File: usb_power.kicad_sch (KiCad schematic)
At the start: 13 parts, among them J1 USB_C_Receptacle_USB2.0_14P, U12 CH340N, U13 TP4056-42-ESOP8

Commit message: HW: Update schematic info frames
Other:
- company: (none) -> A.K.
- title: (none) -> USB and power management
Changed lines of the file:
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@@
 	(generator_version "9.0")
 	(paper "A4")
+	(title_block
+		(title "USB and power management")
+		(date "2025-10-14")
+		(rev "A")
+		(company "A.K.")
+	)
 	(text "TODO:\n\nBattery connector\nDCDC"
 		(exclude_from_sim no)

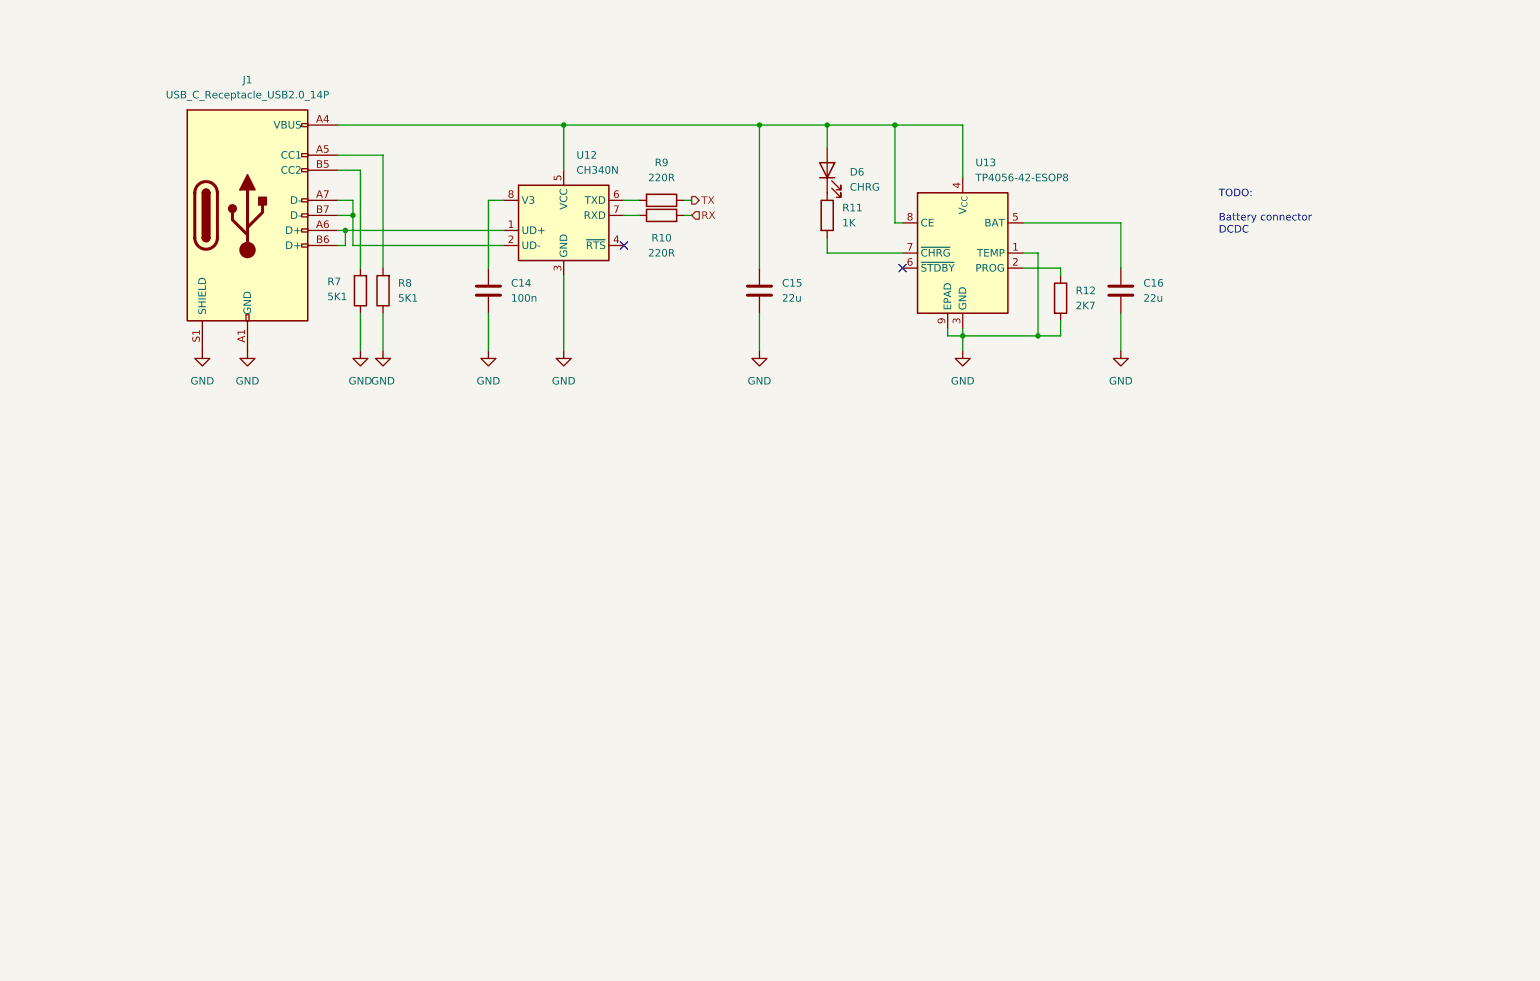
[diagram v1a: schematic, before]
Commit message: HW: Add DC-DC step-up converter
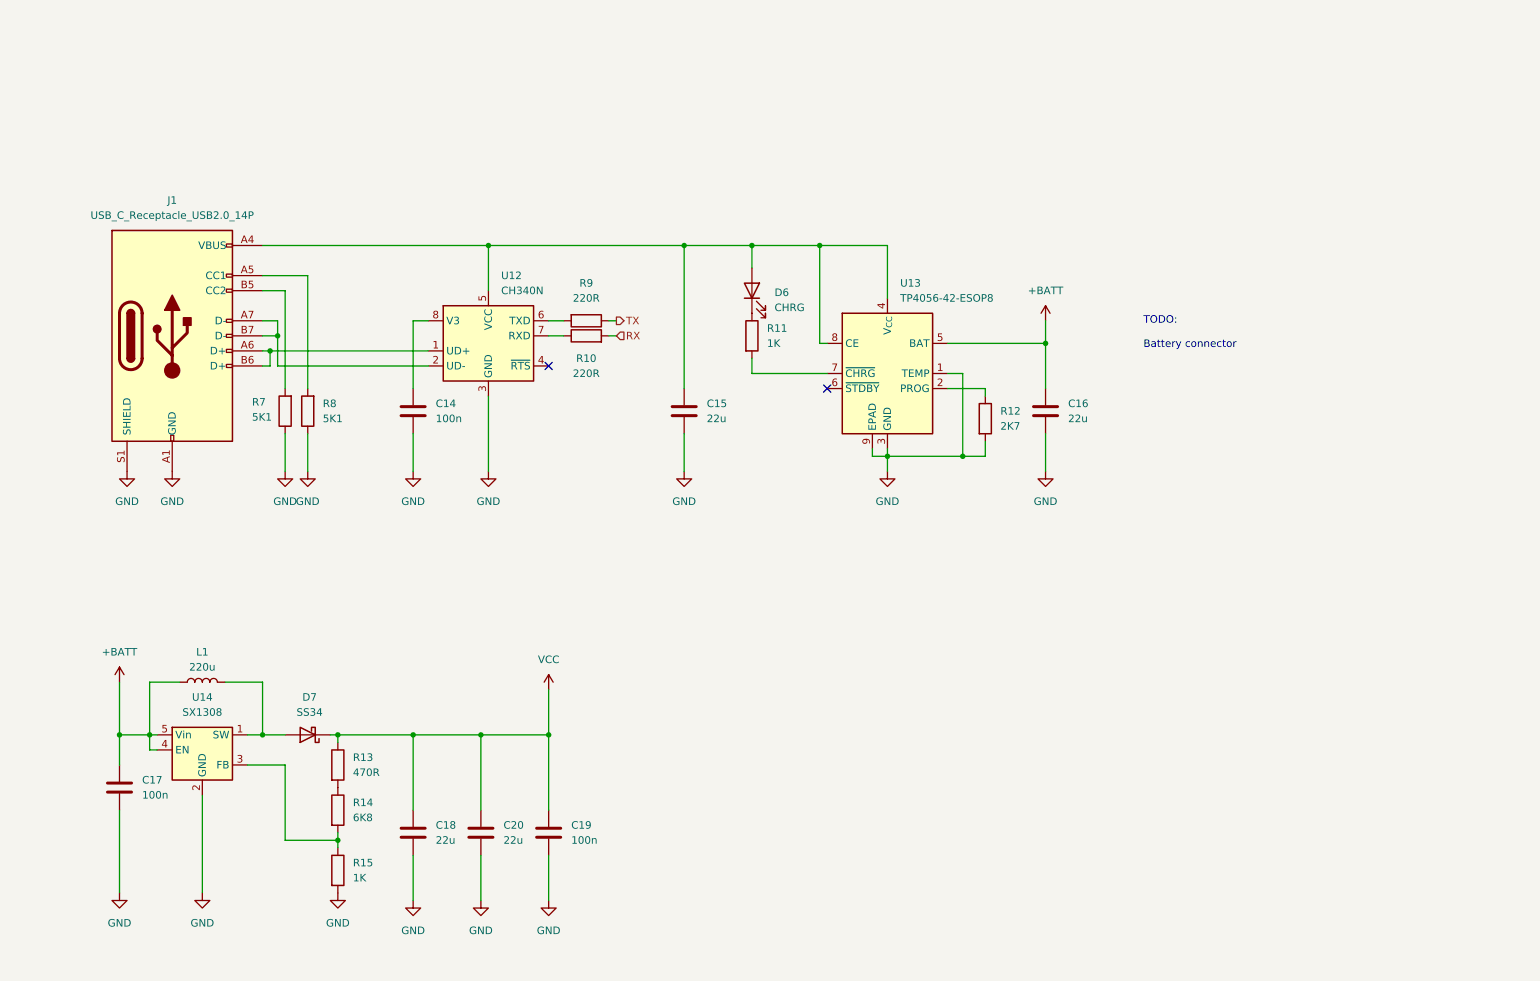
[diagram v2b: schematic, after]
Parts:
- added C17, C19: 100n, Capacitor_SMD:C_0805_2012Metric, symbol Device:C
- added C18, C20: 22u, Capacitor_SMD:C_0805_2012Metric, symbol Device:C
- added D7: SS34, Diode_SMD:D_2010_5025Metric, symbol Device:D_Schottky
- added L1: 220u, Inductor_SMD:L_Sunlord_SWPA6040S, symbol Device:L
- added R13: 470R, Resistor_SMD:R_0805_2012Metric, symbol Device:R
- added R14: 6K8, Resistor_SMD:R_0805_2012Metric, symbol Device:R
- added R15: 1K, Resistor_SMD:R_0805_2012Metric, symbol Device:R
- added U14: SX1308, Package_TO_SOT_SMD:TSOT-23-5, symbol Regulator_Switching:ADP2108AUJ-3.3
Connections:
- net GND: now also C17.1, C18.2, C19.2, C20.2, R15.2, U14.2 (GND)
- net +BATT: now reaches C16.1, U13.5 (BAT)
- net +BATT: now also C17.2, L1.1, U14.4 (EN), U14.5 (Vin)
- new net: R14.2, R15.1, U14.3 (FB)
- new net: D7.2 (A), L1.2, U14.1 (SW)
- new net: R13.2, R14.1
- new net VCC: C18.1, C19.1, C20.1, D7.1 (K), R13.1
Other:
- note added: "TODO: Battery connector"
- note removed: "TODO: Battery connector DCDC"
- moved on the sheet: C14, C15, C16, D6, J1, R10, R11, R12, R7, R8, R9, U12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

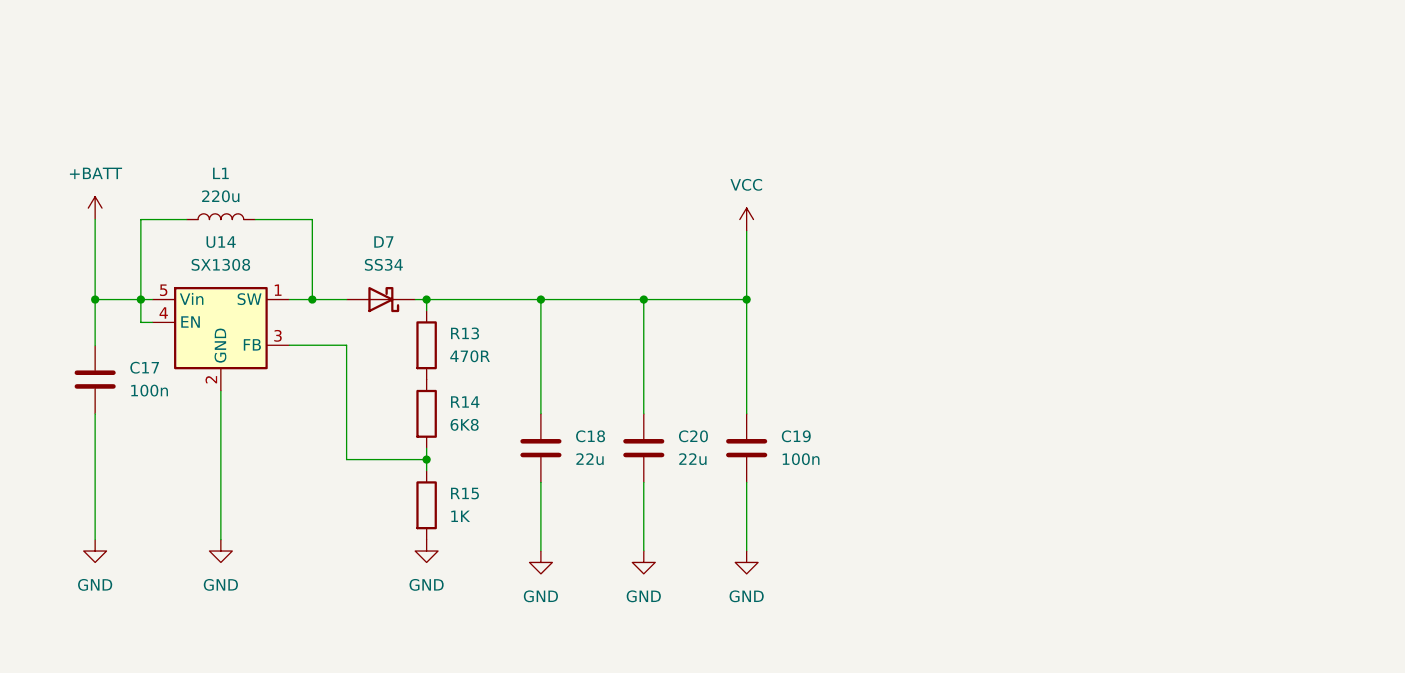
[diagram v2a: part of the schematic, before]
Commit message: HW: Add power switch
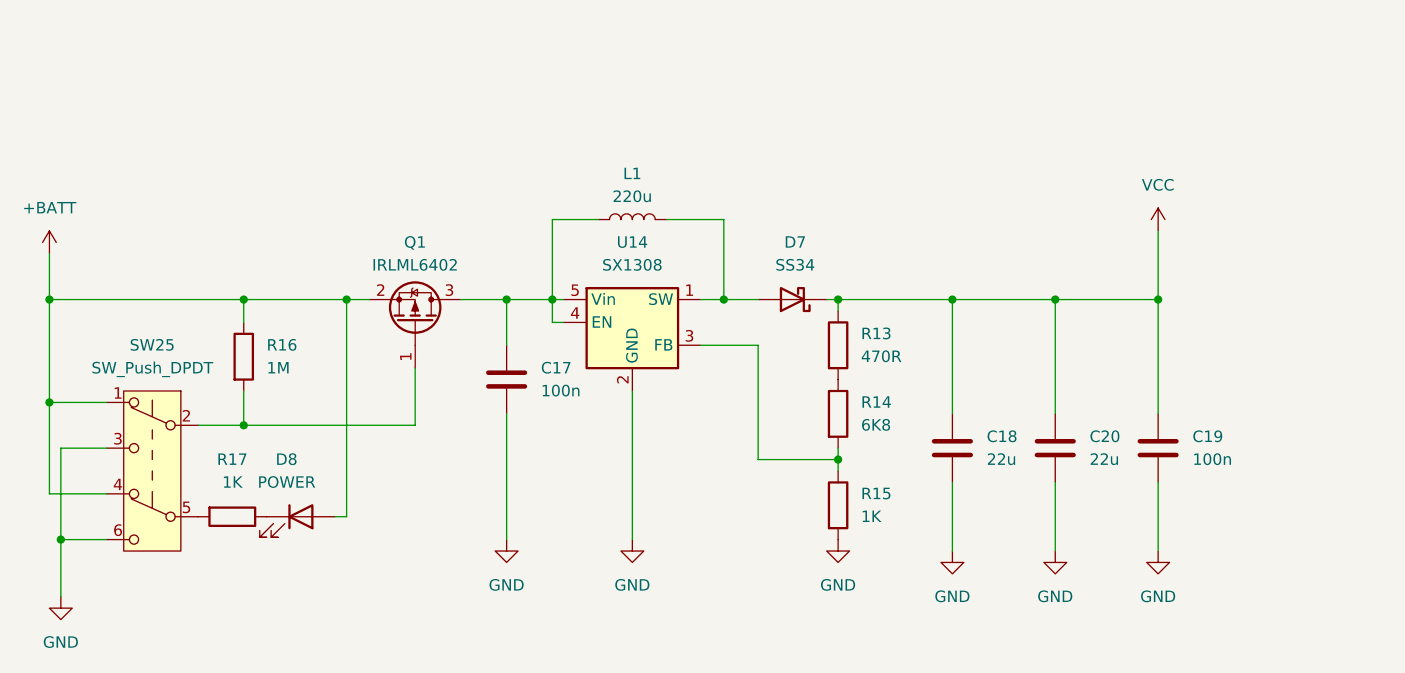
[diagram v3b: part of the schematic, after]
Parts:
- added D8: POWER, LED_SMD:LED_0805_2012Metric, symbol Device:LED
- added Q1: IRLML6402, Package_TO_SOT_SMD:SOT-23, symbol Transistor_FET:IRLML6402
- added R16: 1M, Resistor_SMD:R_0805_2012Metric, symbol Device:R
- added R17: 1K, Resistor_SMD:R_0805_2012Metric, symbol Device:R
- added SW25: SW_Push_DPDT, Button_Switch_THT:SW_CK_JS202011AQN_DPDT_Angled, symbol Switch:SW_Push_DPDT
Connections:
- net +BATT: now also D8.2 (A), Q1.2 (S), R16.1, SW25.1 (A), SW25.4 (A); no longer C17.2, L1.1, U14.4 (EN), U14.5 (Vin)
- net GND: now also SW25.3 (C), SW25.6 (C)
- new net: D8.1 (K), R17.1
- new net: C17.2, L1.1, Q1.3 (D), U14.4 (EN), U14.5 (Vin)
- new net: R17.2, SW25.5 (B)
- new net: Q1.1 (G), R16.2, SW25.2 (B)
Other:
- moved on the sheet: C17, C18, C19, C20, D7, L1, R13, R14, R15, U14

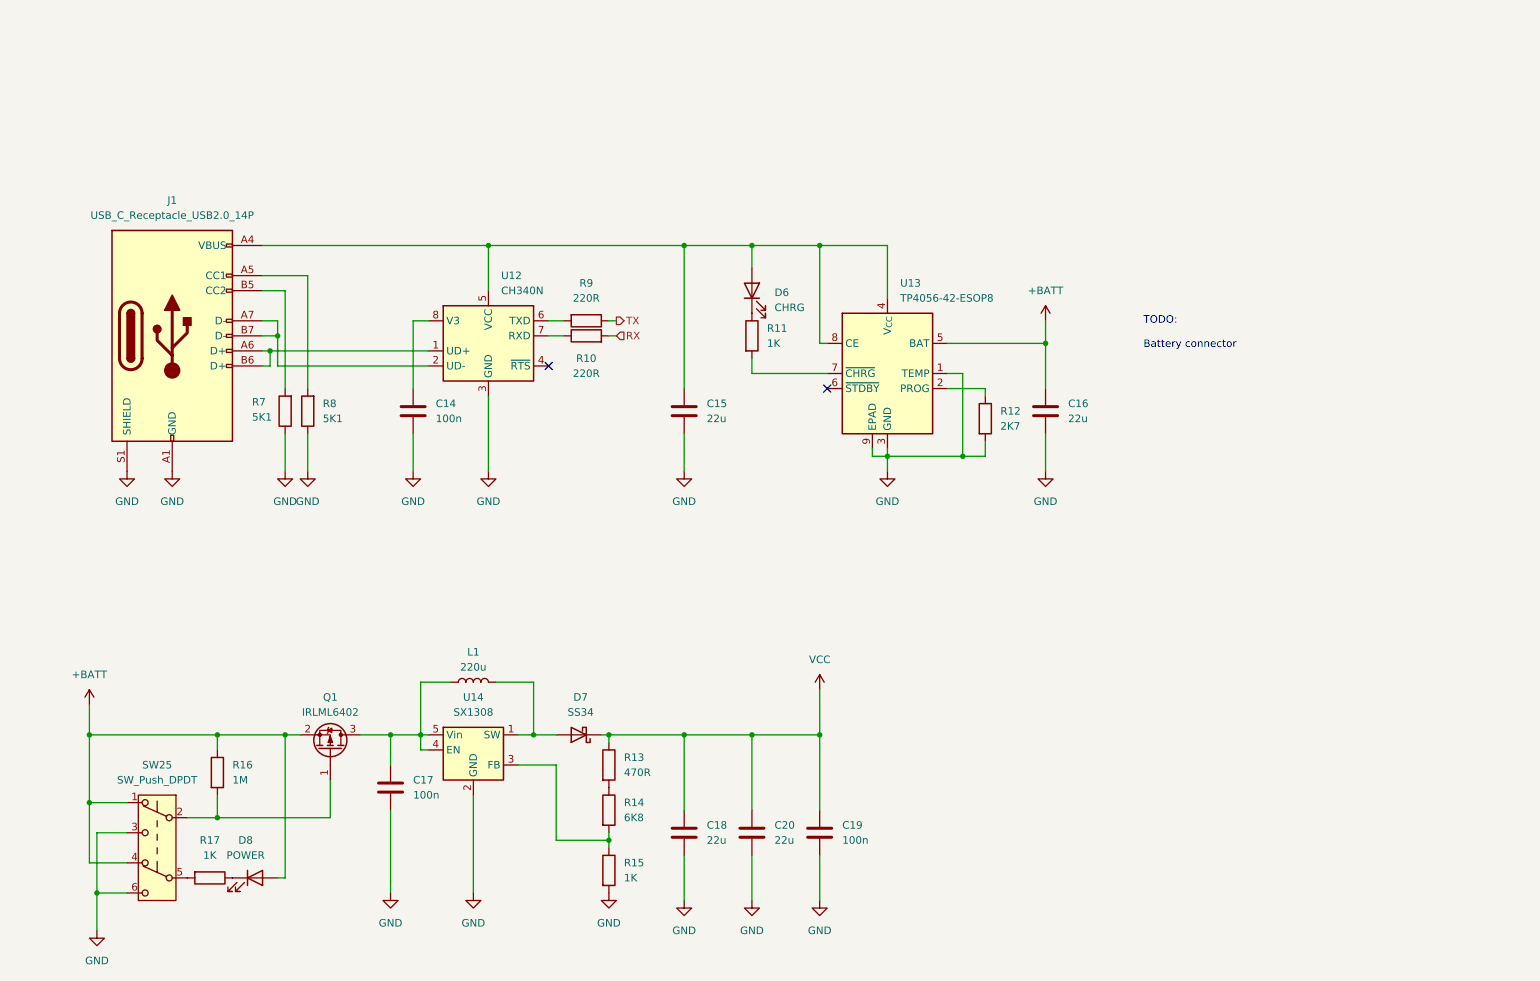
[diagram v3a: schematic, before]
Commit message: HW: Add battery state indicator
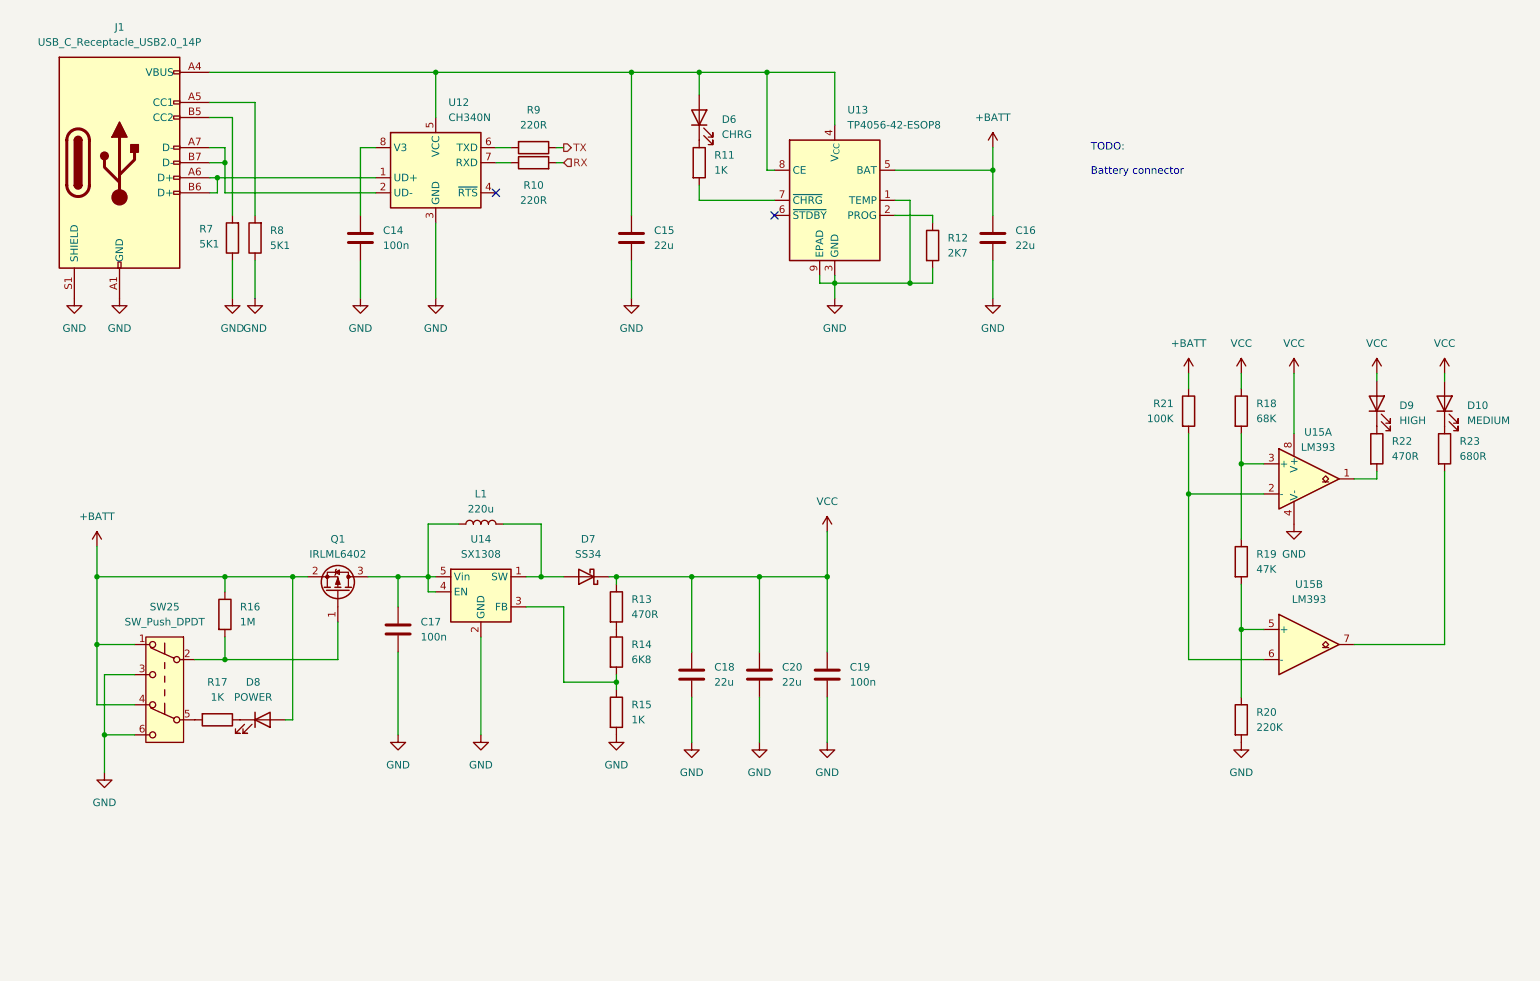
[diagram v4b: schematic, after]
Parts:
- added D10: MEDIUM, LED_SMD:LED_0805_2012Metric, symbol Device:LED
- added D9: HIGH, LED_SMD:LED_0805_2012Metric, symbol Device:LED
- added R18: 68K, Resistor_SMD:R_0805_2012Metric, symbol Device:R
- added R19: 47K, Resistor_SMD:R_0805_2012Metric, symbol Device:R
- added R20: 220K, Resistor_SMD:R_0805_2012Metric, symbol Device:R
- added R21: 100K, Resistor_SMD:R_0805_2012Metric, symbol Device:R
- added R22: 470R, Resistor_SMD:R_0805_2012Metric, symbol Device:R
- added R23: 680R, Resistor_SMD:R_0805_2012Metric, symbol Device:R
- added U15: LM393, Package_SO:SOIC-8_3.9x4.9mm_P1.27mm, symbol Comparator:LM393
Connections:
- net +BATT: now also R21.1
- net GND: now also R20.2, U15.4 (V-)
- net VCC: now also D10.2 (A), D9.2 (A), R18.1, U15.8 (V+)
- new net: R19.2, R20.1, U15.5 (+)
- new net: R21.2, U15.2 (-), U15.6 (-)
- new net: R23.2, U15.7
- new net: R18.2, R19.1, U15.3 (+)
- new net: R22.2, U15.1
- new net: D9.1 (K), R22.1
- new net: D10.1 (K), R23.1
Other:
- moved on the sheet: C14, C15, C16, C17, C18, C19, C20, D6, D7, D8, J1, L1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
